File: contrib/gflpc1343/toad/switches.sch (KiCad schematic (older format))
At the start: 73 parts, among them J1 RJ45, U1 UMN1N, U10 DG408, U11 GSG-LM339, U12 GSG-LM339, U13 GSG-LM339, U14 GSG-LM339, U15 UMP1N, U16 UMP1N, U2 UMN1N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

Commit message: TOAD: power indicator LED, some component selection
git-svn-id: https://svn.code.sf.net/p/goodfet/code@1623 12e2690d-a6be-4b82-a7b7-67c4a43b65c8
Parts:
- U10, U3, U4, U5, U6, U7, U8, U9: Description IC MULTIPLEXER 8X1 16SOIC -> IC MULTIPLEXER 8X1 16TSSOP; Part Number DG408DY-T1-E3 -> DG408LDQ-T1-E3
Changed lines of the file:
@@
-EESchema Schematic File Version 2  date Sun Jul 14 16:16:23 2013
+EESchema Schematic File Version 2  date Mon Jul 15 21:49:01 2013
 LIBS:power
 LIBS:device
@@
 Sheet 2 4
 Title ""
-Date "14 jul 2013"
+Date "16 jul 2013"
 Rev ""
 Comp ""
@@
 F 1 "DG408" V 5050 5850 60  0000 C CNN
 F 4 "Vishay Siliconix" H 5100 5850 60  0001 C CNN "Manufacturer"
-F 5 "DG408DY-T1-E3" H 5100 5850 60  0001 C CNN "Part Number"
-F 6 "IC MULTIPLEXER 8X1 16SOIC" H 5100 5850 60  0001 C CNN "Description"
+F 5 "DG408LDQ-T1-E3" H 5100 5850 60  0001 C CNN "Part Number"
+F 6 "IC MULTIPLEXER 8X1 16TSSOP" H 5100 5850 60  0001 C CNN "Description"
 	1    5100 5850
 	0    1    1    0
@@
 F 1 "DG408" V 6050 5850 60  0000 C CNN
 F 4 "Vishay Siliconix" H 6100 5850 60  0001 C CNN "Manufacturer"
-F 5 "DG408DY-T1-E3" H 6100 5850 60  0001 C CNN "Part Number"
-F 6 "IC MULTIPLEXER 8X1 16SOIC" H 6100 5850 60  0001 C CNN "Description"
+F 5 "DG408LDQ-T1-E3" H 6100 5850 60  0001 C CNN "Part Number"
+F 6 "IC MULTIPLEXER 8X1 16TSSOP" H 6100 5850 60  0001 C CNN "Description"
 	1    6100 5850
 	0    1    1    0
@@
 F 1 "DG408" V 7050 5850 60  0000 C CNN
 F 4 "Vishay Siliconix" H 7100 5850 60  0001 C CNN "Manufacturer"
-F 5 "DG408DY-T1-E3" H 7100 5850 60  0001 C CNN "Part Number"
-F 6 "IC MULTIPLEXER 8X1 16SOIC" H 7100 5850 60  0001 C CNN "Description"
+F 5 "DG408LDQ-T1-E3" H 7100 5850 60  0001 C CNN "Part Number"
+F 6 "IC MULTIPLEXER 8X1 16TSSOP" H 7100 5850 60  0001 C CNN "Description"
 	1    7100 5850
 	0    1    1    0
@@
 F 1 "DG408" V 8050 5850 60  0000 C CNN
 F 4 "Vishay Siliconix" H 8100 5850 60  0001 C CNN "Manufacturer"
-F 5 "DG408DY-T1-E3" H 8100 5850 60  0001 C CNN "Part Number"
-F 6 "IC MULTIPLEXER 8X1 16SOIC" H 8100 5850 60  0001 C CNN "Description"
+F 5 "DG408LDQ-T1-E3" H 8100 5850 60  0001 C CNN "Part Number"
+F 6 "IC MULTIPLEXER 8X1 16TSSOP" H 8100 5850 60  0001 C CNN "Description"
 	1    8100 5850
 	0    1    1    0
@@
 F 1 "DG408" V 9050 5850 60  0000 C CNN
 F 4 "Vishay Siliconix" H 9100 5850 60  0001 C CNN "Manufacturer"
-F 5 "DG408DY-T1-E3" H 9100 5850 60  0001 C CNN "Part Number"
-F 6 "IC MULTIPLEXER 8X1 16SOIC" H 9100 5850 60  0001 C CNN "Description"
+F 5 "DG408LDQ-T1-E3" H 9100 5850 60  0001 C CNN "Part Number"
+F 6 "IC MULTIPLEXER 8X1 16TSSOP" H 9100 5850 60  0001 C CNN "Description"
 	1    9100 5850
 	0    1    1    0
@@
 F 1 "DG408" V 10050 5850 60  0000 C CNN
 F 4 "Vishay Siliconix" H 10100 5850 60  0001 C CNN "Manufacturer"
-F 5 "DG408DY-T1-E3" H 10100 5850 60  0001 C CNN "Part Number"
-F 6 "IC MULTIPLEXER 8X1 16SOIC" H 10100 5850 60  0001 C CNN "Description"
+F 5 "DG408LDQ-T1-E3" H 10100 5850 60  0001 C CNN "Part Number"
+F 6 "IC MULTIPLEXER 8X1 16TSSOP" H 10100 5850 60  0001 C CNN "Description"
 	1    10100 5850
 	0    1    1    0
@@
 F 1 "DG408" V 11050 5850 60  0000 C CNN
 F 4 "Vishay Siliconix" H 11100 5850 60  0001 C CNN "Manufacturer"
-F 5 "DG408DY-T1-E3" H 11100 5850 60  0001 C CNN "Part Number"
-F 6 "IC MULTIPLEXER 8X1 16SOIC" H 11100 5850 60  0001 C CNN "Description"
+F 5 "DG408LDQ-T1-E3" H 11100 5850 60  0001 C CNN "Part Number"
+F 6 "IC MULTIPLEXER 8X1 16TSSOP" H 11100 5850 60  0001 C CNN "Description"
 	1    11100 5850
 	0    1    1    0
@@
 F 1 "DG408" V 12050 5850 60  0000 C CNN
 F 4 "Vishay Siliconix" H 12100 5850 60  0001 C CNN "Manufacturer"
-F 5 "DG408DY-T1-E3" H 12100 5850 60  0001 C CNN "Part Number"
-F 6 "IC MULTIPLEXER 8X1 16SOIC" H 12100 5850 60  0001 C CNN "Description"
+F 5 "DG408LDQ-T1-E3" H 12100 5850 60  0001 C CNN "Part Number"
+F 6 "IC MULTIPLEXER 8X1 16TSSOP" H 12100 5850 60  0001 C CNN "Description"
 	1    12100 5850
 	0    1    1    0

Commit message: TOAD: comparator voltage dividers
git-svn-id: https://svn.code.sf.net/p/goodfet/code@1624 12e2690d-a6be-4b82-a7b7-67c4a43b65c8
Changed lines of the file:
@@
-EESchema Schematic File Version 2  date Mon Jul 15 21:49:01 2013
+EESchema Schematic File Version 2  date Thu Jul 18 16:05:09 2013
 LIBS:power
 LIBS:device
@@
 Sheet 2 4
 Title ""
-Date "16 jul 2013"
+Date "18 jul 2013"
 Rev ""
 Comp ""
@@
 $EndComp
 Wire Wire Line
-	5250 5400 5250 1200
-Wire Wire Line
-	5250 1200 5250 850
+	5250 850  5250 5400
 Wire Wire Line
 	5250 850  6650 850
@@
 	6250 5400 6250 1850
 Wire Wire Line
-	6150 1850 6250 1850
-Wire Wire Line
-	6250 1850 6650 1850
+	6150 1850 6650 1850
 Wire Wire Line
 	6650 1850 6650 1750
@@
 	7250 5400 7250 1850
 Wire Wire Line
-	6850 1850 7250 1850
-Wire Wire Line
-	7250 1850 7350 1850
+	6850 1850 7350 1850
 Wire Wire Line
 	6850 1850 6850 1750
 Wire Wire Line
-	8250 850  8250 1200
-Wire Wire Line
-	8250 1200 8250 5400
+	8250 850  8250 5400
 Wire Wire Line
 	8250 850  6850 850
@@
 	6850 850  6850 950
 Wire Wire Line
-	9250 5400 9250 1200
-Wire Wire Line
-	9250 1200 9250 850
+	9250 850  9250 5400
 Wire Wire Line
 	9250 850  10650 850
@@
 	10250 5400 10250 1850
 Wire Wire Line
-	10150 1850 10250 1850
-Wire Wire Line
-	10250 1850 10650 1850
+	10150 1850 10650 1850
 Wire Wire Line
 	10650 1850 10650 1750
@@
 	11250 5400 11250 1850
 Wire Wire Line
-	10850 1850 11250 1850
-Wire Wire Line
-	11250 1850 11350 1850
+	10850 1850 11350 1850
 Wire Wire Line
 	10850 1850 10850 1750
 Wire Wire Line
-	12250 5400 12250 1200
-Wire Wire Line
-	12250 1200 12250 850
+	12250 850  12250 5400
 Wire Wire Line
 	12250 850  10850 850
@@
 	10850 850  10850 950
 Wire Wire Line
-	5150 6300 5150 9700
-Wire Wire Line
-	5150 9700 5150 10100
+	5150 6300 5150 10100
 Wire Wire Line
 	5150 10100 6550 10100
@@
 	6150 6300 6150 9100
 Wire Wire Line
-	6050 9100 6150 9100
-Wire Wire Line
-	6150 9100 6550 9100
+	6050 9100 6550 9100
 Wire Wire Line
 	6550 9100 6550 9200
@@
 	7150 6300 7150 9100
 Wire Wire Line
-	6750 9100 7150 9100
-Wire Wire Line
-	7150 9100 7250 9100
+	6750 9100 7250 9100
 Wire Wire Line
 	6750 9100 6750 9200
 Wire Wire Line
-	8150 6300 8150 9700
-Wire Wire Line
-	8150 9700 8150 10100
+	8150 6300 8150 10100
 Wire Wire Line
 	8150 10100 6750 10100
@@
 	6750 10100 6750 10000
 Wire Wire Line
-	9150 6300 9150 9700
-Wire Wire Line
-	9150 9700 9150 10100
+	9150 6300 9150 10100
 Wire Wire Line
 	9150 10100 10550 10100
@@
 	10150 6300 10150 9100
 Wire Wire Line
-	10050 9100 10150 9100
-Wire Wire Line
-	10150 9100 10550 9100
+	10050 9100 10550 9100
 Wire Wire Line
 	10550 9100 10550 9200
@@
 	11150 6300 11150 9100
 Wire Wire Line
-	10750 9100 11150 9100
-Wire Wire Line
-	11150 9100 11250 9100
+	10750 9100 11250 9100
 Wire Wire Line
 	10750 9100 10750 9200
 Wire Wire Line
-	12150 6300 12150 9700
-Wire Wire Line
-	12150 9700 12150 10100
+	12150 6300 12150 10100
 Wire Wire Line
 	12150 10100 10750 10100
@@
 	12450 4350 14150 4350
 Wire Wire Line
-	12350 4250 12350 4500
-Wire Wire Line
-	12350 4500 12350 5400
+	12350 4250 12350 5400
 Wire Wire Line
 	12350 4250 14150 4250
@@
 	11450 4150 11450 5400
 Wire Wire Line
-	11350 4050 11350 4500
-Wire Wire Line
-	11350 4500 11350 5400
+	11350 4050 11350 5400
 Wire Wire Line
 	11350 4050 14150 4050
@@
 	10450 3950 10450 5400
 Wire Wire Line
-	10350 3850 10350 4500
-Wire Wire Line
-	10350 4500 10350 5400
+	10350 3850 10350 5400
 Wire Wire Line
 	10350 3850 14150 3850
@@
 	14150 3650 9350 3650
 Wire Wire Line
-	9350 3650 9350 4500
-Wire Wire Line
-	9350 4500 9350 5400
+	9350 3650 9350 5400
 Wire Wire Line
 	14150 3550 8450 3550
@@
 	8450 3550 8450 5400
 Wire Wire Line
-	8350 3450 8350 4500
-Wire Wire Line
-	8350 4500 8350 5400
+	8350 3450 8350 5400
 Wire Wire Line
 	8350 3450 14150 3450
@@
 	7450 3350 7450 5400
 Wire Wire Line
-	7350 3250 7350 4500
-Wire Wire Line
-	7350 4500 7350 5400
+	7350 3250 7350 5400
 Wire Wire Line
 	7350 3250 14150 3250
@@
 	6450 3150 6450 5400
 Wire Wire Line
-	6350 3050 6350 4500
-Wire Wire Line
-	6350 4500 6350 5400
+	6350 3050 6350 5400
 Wire Wire Line
 	6350 3050 14150 3050
@@
 	5450 2950 5450 5400
 Wire Wire Line
-	5350 2850 5350 4500
-Wire Wire Line
-	5350 4500 5350 5400
+	5350 2850 5350 5400
 Wire Wire Line
 	5350 2850 14150 2850
@@
 	4750 6600 4750 6300
 Wire Wire Line
-	750  6600 2550 6600
-Wire Wire Line
-	2550 6600 4750 6600
-Wire Wire Line
-	850  6700 2650 6700
-Wire Wire Line
-	2650 6700 5750 6700
+	750  6600 4750 6600
+Wire Wire Line
+	850  6700 5750 6700
 Wire Wire Line
 	5750 6700 5750 6300
@@
 	6750 6800 6750 6300
 Wire Wire Line
-	2350 6800 4150 6800
-Wire Wire Line
-	4150 6800 6750 6800
-Wire Wire Line
-	2450 6900 4250 6900
-Wire Wire Line
-	4250 6900 7750 6900
+	2350 6800 6750 6800
+Wire Wire Line
+	2450 6900 7750 6900
 Wire Wire Line
 	7750 6900 7750 6300
 Wire Wire Line
-	2450 7000 4250 7000
-Wire Wire Line
-	4250 7000 8750 7000
+	2450 7000 8750 7000
 Wire Wire Line
 	8750 7000 8750 6300
@@
 	9750 7100 9750 6300
 Wire Wire Line
-	2350 7100 4150 7100
-Wire Wire Line
-	4150 7100 9750 7100
-Wire Wire Line
-	850  7200 2650 7200
-Wire Wire Line
-	2650 7200 10750 7200
+	2350 7100 9750 7100
+Wire Wire Line
+	850  7200 10750 7200
 Wire Wire Line
 	10750 7200 10750 6300
@@
 	11750 7300 11750 6300
 Wire Wire Line
-	750  7300 2550 7300
-Wire Wire Line
-	2550 7300 11750 7300
+	750  7300 11750 7300
 $Comp
 L GSG-LM339 U11
@@
 	900  9500 900  9600
 Wire Wire Line
-	900  9600 1000 9600
-Wire Wire Line
-	1000 9600 1400 9600
-Wire Wire Line
-	1400 9600 1800 9600
-Wire Wire Line
-	1800 9600 2200 9600
+	900  9600 2200 9600
 Wire Wire Line
 	1000 9600 1000 9700
@@
 	1000 10100 1000 10200
 Wire Wire Line
-	900  10200 1000 10200
-Wire Wire Line
-	1000 10200 1400 10200
-Wire Wire Line
-	1400 10200 1800 10200
-Wire Wire Line
-	1800 10200 2200 10200
+	900  10200 2200 10200
 Wire Wire Line
 	900  10200 900  10300
@@
 	2700 9500 2700 9600
 Wire Wire Line
-	2700 9600 2800 9600
-Wire Wire Line
-	2800 9600 3200 9600
-Wire Wire Line
-	3200 9600 3600 9600
-Wire Wire Line
-	3600 9600 4000 9600
+	2700 9600 4000 9600
 Wire Wire Line
 	2800 9600 2800 9700
@@
 	2800 10100 2800 10200
 Wire Wire Line
-	2700 10200 2800 10200
-Wire Wire Line
-	2800 10200 3200 10200
-Wire Wire Line
-	3200 10200 3600 10200
-Wire Wire Line
-	3600 10200 4000 10200
+	2700 10200 4000 10200
 Wire Wire Line
 	2700 10200 2700 10300

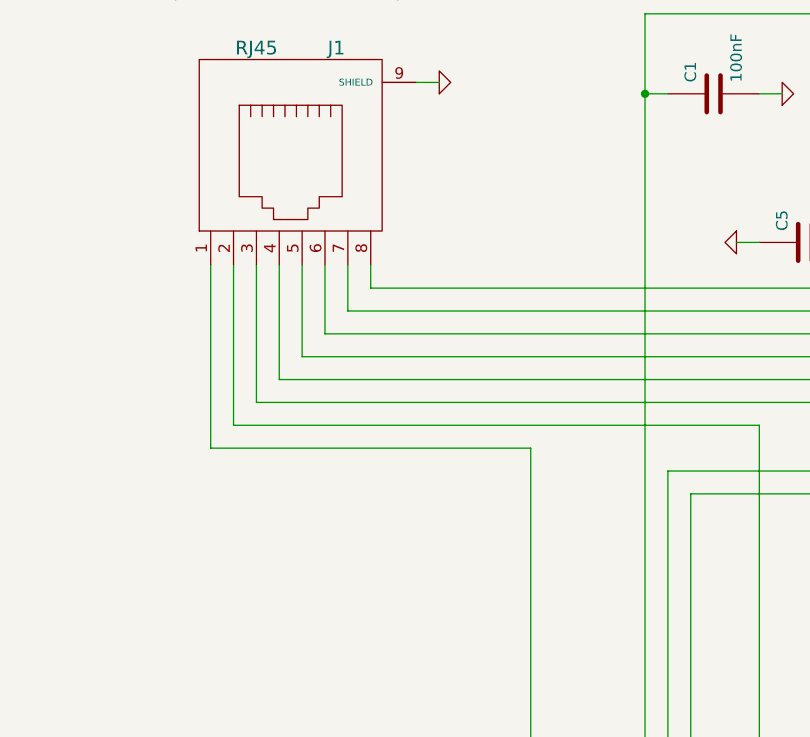
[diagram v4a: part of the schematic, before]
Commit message: completed TOAD design
git-svn-id: https://svn.code.sf.net/p/goodfet/code@1656 12e2690d-a6be-4b82-a7b7-67c4a43b65c8
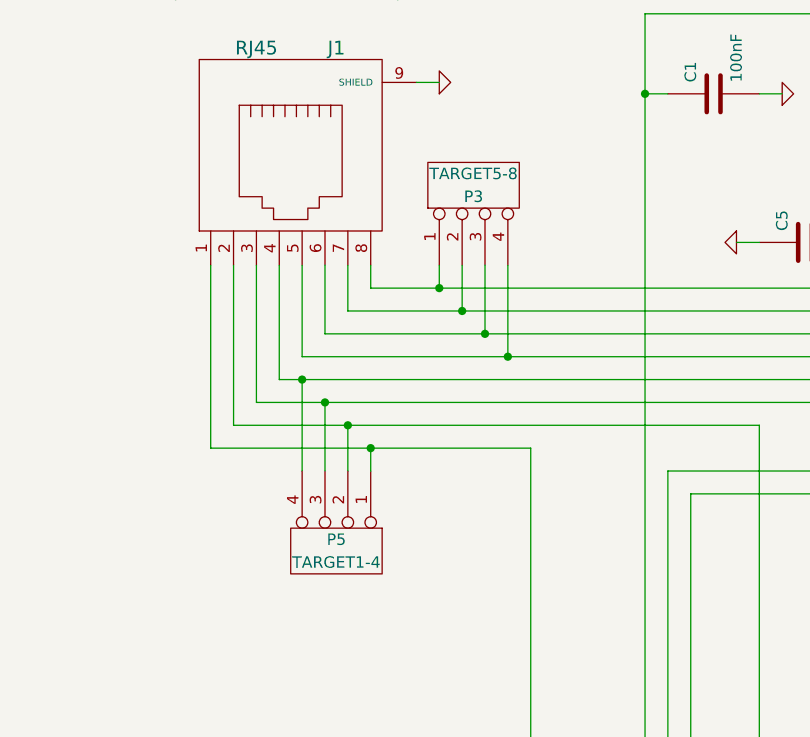
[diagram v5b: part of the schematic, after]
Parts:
- added P3: TARGET5-8, symbol CONN_4
- added P5: TARGET1-4, symbol CONN_4
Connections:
- net at J1.1, U3.8 (D): now also P5.1 (P1)
- net at J1.2, U4.8 (D): now also P5.2 (P2)
- net at J1.3, U5.8 (D): now also P5.3 (P3)
- net at J1.4, U6.8 (D): now also P5.4 (P4)
- net at J1.5, U7.8 (D): now also P3.4 (P4)
- net at J1.6, U8.8 (D): now also P3.3 (P3)
- net at J1.7, U9.8 (D): now also P3.2 (P2)
- net at J1.8, U10.8 (D): now also P3.1 (P1)
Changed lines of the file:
@@
-EESchema Schematic File Version 2  date Thu Jul 18 17:37:42 2013
+EESchema Schematic File Version 2  date Mon Jul 22 09:26:32 2013
 LIBS:power
 LIBS:device
@@
 Sheet 2 4
 Title ""
-Date "18 jul 2013"
+Date "22 jul 2013"
 Rev ""
 Comp ""
@@
 Text GLabel 14150 8900 2    40   Input ~ 0
 SW1A2
+$Comp
+L CONN_4 P3
+U 1 1 51EC4A97
+P 4500 1600
+F 0 "P3" V 4450 1600 50  0000 C CNN
+F 1 "TARGET5-8" V 4550 1600 50  0000 C CNN
+	1    4500 1600
+	0    -1   -1   0
+$EndComp
+$Comp
+L CONN_4 P5
+U 1 1 51EC4AA4
+P 3900 3200
+F 0 "P5" V 3850 3200 50  0000 C CNN
+F 1 "TARGET1-4" V 3950 3200 50  0000 C CNN
+	1    3900 3200
+	0    1    1    0
+$EndComp
+Wire Wire Line
+	4050 2850 4050 2750
+Connection ~ 4050 2750
+Wire Wire Line
+	3950 2850 3950 2650
+Connection ~ 3950 2650
+Wire Wire Line
+	3850 2850 3850 2550
+Connection ~ 3850 2550
+Wire Wire Line
+	3750 2850 3750 2450
+Connection ~ 3750 2450
+Wire Wire Line
+	4350 1950 4350 2050
+Connection ~ 4350 2050
+Wire Wire Line
+	4450 1950 4450 2150
+Connection ~ 4450 2150
+Wire Wire Line
+	4550 1950 4550 2250
+Connection ~ 4550 2250
+Wire Wire Line
+	4650 1950 4650 2350
+Connection ~ 4650 2350
 $EndSCHEMATC

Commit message: TOAD: fixed part numbers for DG408/DG409
git-svn-id: https://svn.code.sf.net/p/goodfet/code@1660 12e2690d-a6be-4b82-a7b7-67c4a43b65c8
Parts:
- U10, U3, U4, U5, U6, U7, U8, U9: Part Number DG408LDQ-T1-E3 -> DG408DQ-T1-E3
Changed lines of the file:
@@
 F 1 "DG408" V 5050 5850 60  0000 C CNN
 F 4 "Vishay Siliconix" H 5100 5850 60  0001 C CNN "Manufacturer"
-F 5 "DG408LDQ-T1-E3" H 5100 5850 60  0001 C CNN "Part Number"
+F 5 "DG408DQ-T1-E3" H 5100 5850 60  0001 C CNN "Part Number"
 F 6 "IC MULTIPLEXER 8X1 16TSSOP" H 5100 5850 60  0001 C CNN "Description"
 	1    5100 5850
@@
 F 1 "DG408" V 6050 5850 60  0000 C CNN
 F 4 "Vishay Siliconix" H 6100 5850 60  0001 C CNN "Manufacturer"
-F 5 "DG408LDQ-T1-E3" H 6100 5850 60  0001 C CNN "Part Number"
+F 5 "DG408DQ-T1-E3" H 6100 5850 60  0001 C CNN "Part Number"
 F 6 "IC MULTIPLEXER 8X1 16TSSOP" H 6100 5850 60  0001 C CNN "Description"
 	1    6100 5850
@@
 F 1 "DG408" V 7050 5850 60  0000 C CNN
 F 4 "Vishay Siliconix" H 7100 5850 60  0001 C CNN "Manufacturer"
-F 5 "DG408LDQ-T1-E3" H 7100 5850 60  0001 C CNN "Part Number"
+F 5 "DG408DQ-T1-E3" H 7100 5850 60  0001 C CNN "Part Number"
 F 6 "IC MULTIPLEXER 8X1 16TSSOP" H 7100 5850 60  0001 C CNN "Description"
 	1    7100 5850
@@
 F 1 "DG408" V 8050 5850 60  0000 C CNN
 F 4 "Vishay Siliconix" H 8100 5850 60  0001 C CNN "Manufacturer"
-F 5 "DG408LDQ-T1-E3" H 8100 5850 60  0001 C CNN "Part Number"
+F 5 "DG408DQ-T1-E3" H 8100 5850 60  0001 C CNN "Part Number"
 F 6 "IC MULTIPLEXER 8X1 16TSSOP" H 8100 5850 60  0001 C CNN "Description"
 	1    8100 5850
@@
 F 1 "DG408" V 9050 5850 60  0000 C CNN
 F 4 "Vishay Siliconix" H 9100 5850 60  0001 C CNN "Manufacturer"
-F 5 "DG408LDQ-T1-E3" H 9100 5850 60  0001 C CNN "Part Number"
+F 5 "DG408DQ-T1-E3" H 9100 5850 60  0001 C CNN "Part Number"
 F 6 "IC MULTIPLEXER 8X1 16TSSOP" H 9100 5850 60  0001 C CNN "Description"
 	1    9100 5850
@@
 F 1 "DG408" V 10050 5850 60  0000 C CNN
 F 4 "Vishay Siliconix" H 10100 5850 60  0001 C CNN "Manufacturer"
-F 5 "DG408LDQ-T1-E3" H 10100 5850 60  0001 C CNN "Part Number"
+F 5 "DG408DQ-T1-E3" H 10100 5850 60  0001 C CNN "Part Number"
 F 6 "IC MULTIPLEXER 8X1 16TSSOP" H 10100 5850 60  0001 C CNN "Description"
 	1    10100 5850
@@
 F 1 "DG408" V 11050 5850 60  0000 C CNN
 F 4 "Vishay Siliconix" H 11100 5850 60  0001 C CNN "Manufacturer"
-F 5 "DG408LDQ-T1-E3" H 11100 5850 60  0001 C CNN "Part Number"
+F 5 "DG408DQ-T1-E3" H 11100 5850 60  0001 C CNN "Part Number"
 F 6 "IC MULTIPLEXER 8X1 16TSSOP" H 11100 5850 60  0001 C CNN "Description"
 	1    11100 5850
@@
 F 1 "DG408" V 12050 5850 60  0000 C CNN
 F 4 "Vishay Siliconix" H 12100 5850 60  0001 C CNN "Manufacturer"
-F 5 "DG408LDQ-T1-E3" H 12100 5850 60  0001 C CNN "Part Number"
+F 5 "DG408DQ-T1-E3" H 12100 5850 60  0001 C CNN "Part Number"
 F 6 "IC MULTIPLEXER 8X1 16TSSOP" H 12100 5850 60  0001 C CNN "Description"
 	1    12100 5850
